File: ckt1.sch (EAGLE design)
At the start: 16 parts, among them J1 POWER_JACKSLT, M1 WIRELESS-NRF24L01-PA-EXT, U1 328P

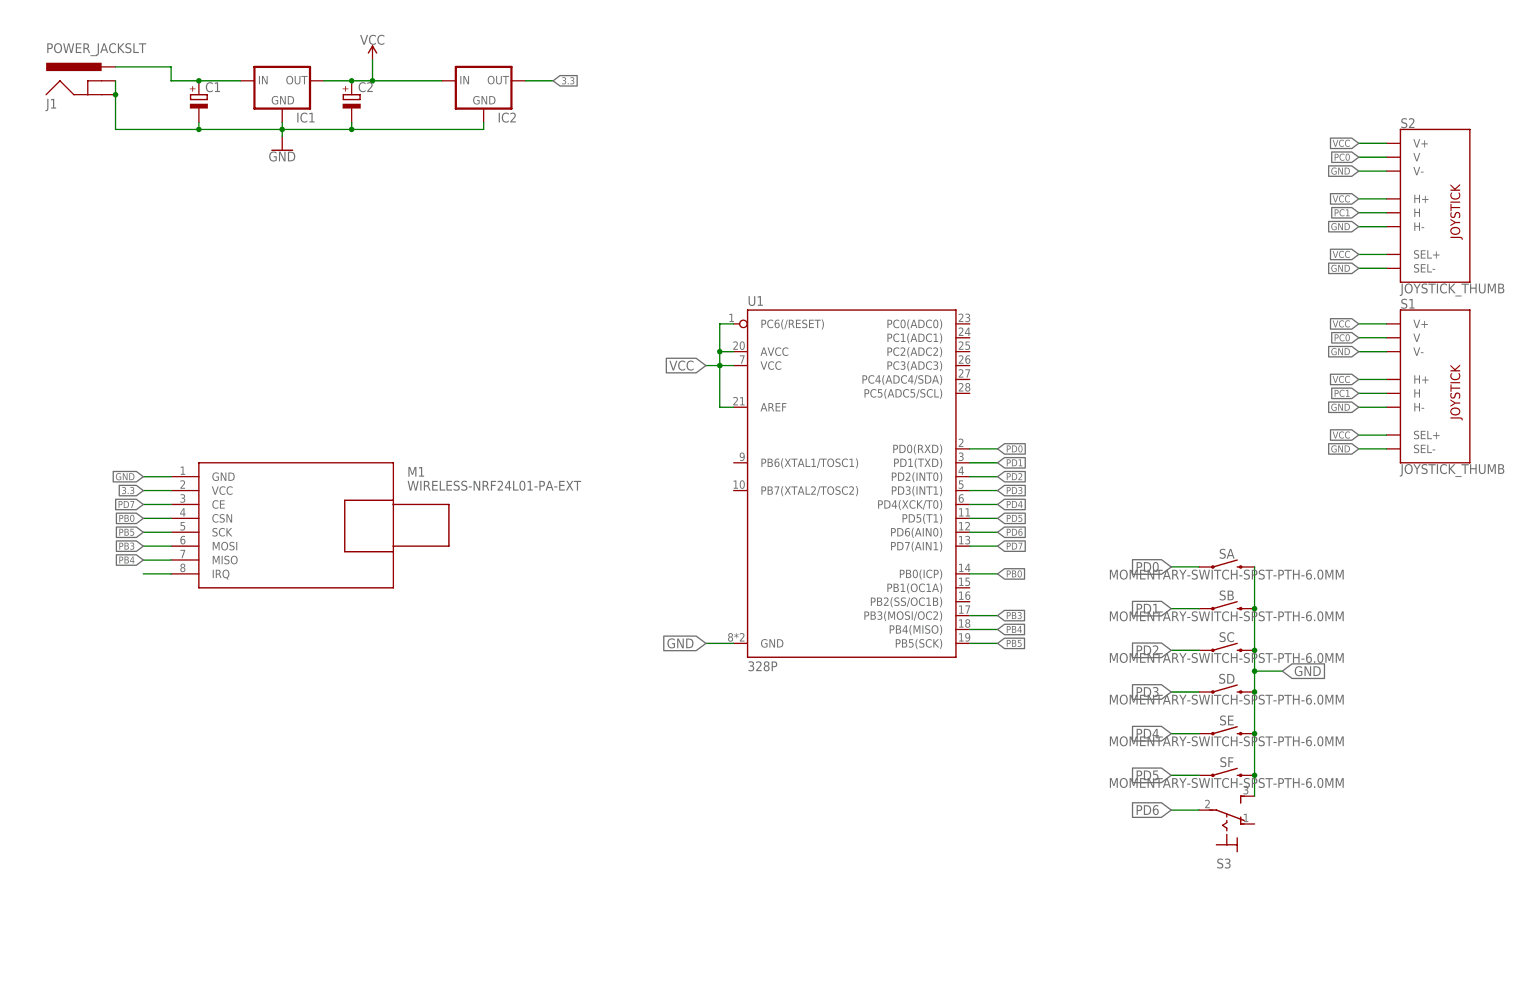
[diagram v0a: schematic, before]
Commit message: Formatting schematic and adding XTAL
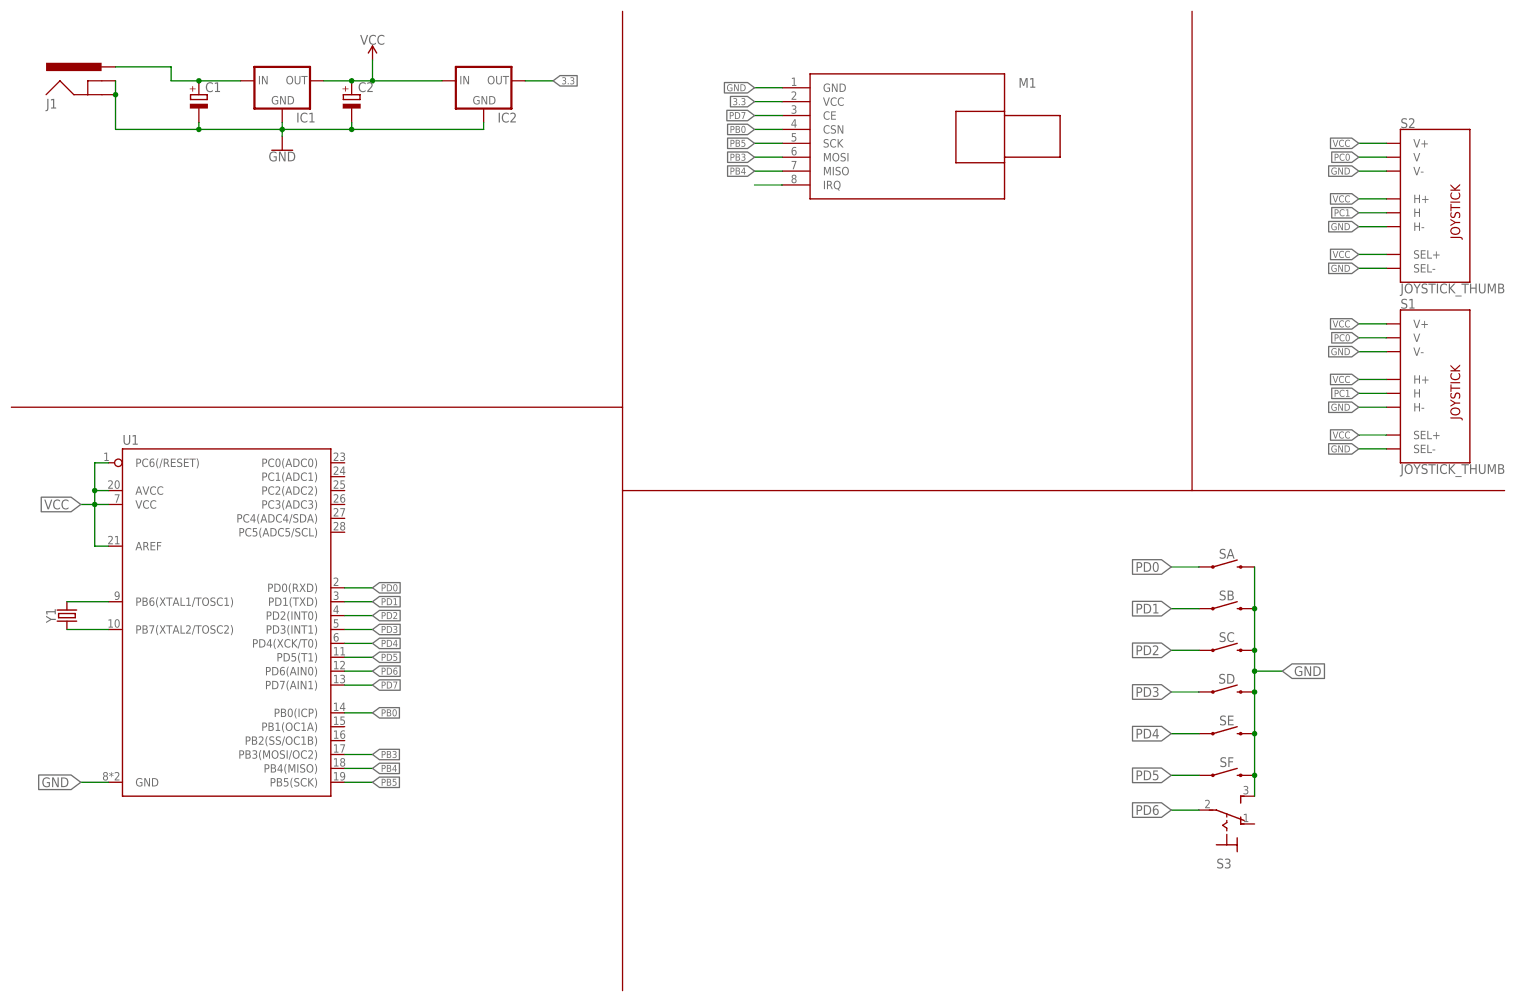
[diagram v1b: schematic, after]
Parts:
- added Y1: (no value), SparkFun-Clocks:CRYSTALPTH-HC49US
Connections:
- new net N$1: U1.PB6(XTAL1/TOSC1), Y1.2
- new net N$3: U1.PB7(XTAL2/TOSC2), Y1.1
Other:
- moved on the sheet: M1, U1

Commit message: Some changes to the board file
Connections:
- new net PC2: S1.V, U1.PC2(ADC2)
- new net PC3: S1.H, U1.PC3(ADC3)
- net GND: no longer S1.SEL-, S2.SEL-
- net PC0: now also U1.PC0(ADC0); no longer S1.V
- net PC1: now also U1.PC1(ADC1); no longer S1.H
- net VCC: no longer S1.SEL+, S2.SEL+
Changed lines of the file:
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@@
 <setting verticaltext="up"/>
 </settings>
-<grid distance="0.05" unitdist="inch" unit="inch" style="lines" multiple="1" display="yes" altdistance="0.005" altunitdist="inch" altunit="inch"/>
+<grid distance="0.1" unitdist="inch" unit="inch" style="lines" multiple="1" display="no" altdistance="0.01" altunitdist="inch" altunit="inch"/>
 <layers>
 <layer number="1" name="Top" color="4" fill="1" visible="no" active="no"/>
@@
 </segment>
 <segment>
-<pinref part="S2" gate="G$1" pin="SEL+"/>
-<wire x1="251.46" y1="134.62" x2="246.38" y2="134.62" width="0.1524" layer="91"/>
-<label x="246.38" y="134.62" size="1.27" layer="95" rot="R180" xref="yes"/>
-</segment>
-<segment>
 <pinref part="S1" gate="G$1" pin="V+"/>
 <wire x1="251.46" y1="121.92" x2="246.38" y2="121.92" width="0.1524" layer="91"/>
@@
 <wire x1="251.46" y1="111.76" x2="246.38" y2="111.76" width="0.1524" layer="91"/>
 <label x="246.38" y="111.76" size="1.27" layer="95" rot="R180" xref="yes"/>
-</segment>
-<segment>
-<pinref part="S1" gate="G$1" pin="SEL+"/>
-<wire x1="251.46" y1="101.6" x2="246.38" y2="101.6" width="0.1524" layer="91"/>
-<label x="246.38" y="101.6" size="1.27" layer="95" rot="R180" xref="yes"/>
 </segment>
 <segment>
@@
 </segment>
 <segment>
-<pinref part="S2" gate="G$1" pin="SEL-"/>
-<wire x1="251.46" y1="132.08" x2="246.38" y2="132.08" width="0.1524" layer="91"/>
-<label x="246.38" y="132.08" size="1.27" layer="95" rot="R180" xref="yes"/>
-</segment>
-<segment>
 <pinref part="S1" gate="G$1" pin="V-"/>
 <wire x1="251.46" y1="116.84" x2="246.38" y2="116.84" width="0.1524" layer="91"/>
@@
 <wire x1="251.46" y1="106.68" x2="246.38" y2="106.68" width="0.1524" layer="91"/>
 <label x="246.38" y="106.68" size="1.27" layer="95" rot="R180" xref="yes"/>
-</segment>
-<segment>
-<pinref part="S1" gate="G$1" pin="SEL-"/>
-<wire x1="251.46" y1="99.06" x2="246.38" y2="99.06" width="0.1524" layer="91"/>
-<label x="246.38" y="99.06" size="1.27" layer="95" rot="R180" xref="yes"/>
 </segment>
 <segment>
@@
 </segment>
 <segment>
-<pinref part="S1" gate="G$1" pin="V"/>
-<wire x1="251.46" y1="119.38" x2="246.38" y2="119.38" width="0.1524" layer="91"/>
-<label x="246.38" y="119.38" size="1.27" layer="95" rot="R180" xref="yes"/>
+<pinref part="U1" gate="U1" pin="PC0(ADC0)"/>
+<wire x1="60.96" y1="96.52" x2="66.04" y2="96.52" width="0.1524" layer="91"/>
+<label x="66.04" y="96.52" size="1.27" layer="95" xref="yes"/>
 </segment>
 </net>
@@
 </segment>
 <segment>
-<pinref part="S1" gate="G$1" pin="H"/>
-<wire x1="251.46" y1="109.22" x2="246.38" y2="109.22" width="0.1524" layer="91"/>
-<label x="246.38" y="109.22" size="1.27" layer="95" rot="R180" xref="yes"/>
+<pinref part="U1" gate="U1" pin="PC1(ADC1)"/>
+<wire x1="60.96" y1="93.98" x2="66.04" y2="93.98" width="0.1524" layer="91"/>
+<label x="66.04" y="93.98" size="1.27" layer="95" xref="yes"/>
 </segment>
 </net>
@@
 </segment>
 </net>
+<net name="PC2" class="0">
+<segment>
+<pinref part="U1" gate="U1" pin="PC2(ADC2)"/>
+<wire x1="60.96" y1="91.44" x2="66.04" y2="91.44" width="0.1524" layer="91"/>
+<label x="66.04" y="91.44" size="1.27" layer="95" xref="yes"/>
+</segment>
+<segment>
+<pinref part="S1" gate="G$1" pin="V"/>
+<wire x1="251.46" y1="119.38" x2="246.38" y2="119.38" width="0.1524" layer="91"/>
+<label x="246.38" y="119.38" size="1.27" layer="95" rot="R180" xref="yes"/>
+</segment>
+</net>
+<net name="PC3" class="0">
+<segment>
+<pinref part="U1" gate="U1" pin="PC3(ADC3)"/>
+<wire x1="60.96" y1="88.9" x2="66.04" y2="88.9" width="0.1524" layer="91"/>
+<label x="66.04" y="88.9" size="1.27" layer="95" xref="yes"/>
+</segment>
+<segment>
+<pinref part="S1" gate="G$1" pin="H"/>
+<wire x1="251.46" y1="109.22" x2="246.38" y2="109.22" width="0.1524" layer="91"/>
+<label x="246.38" y="109.22" size="1.27" layer="95" rot="R180" xref="yes"/>
+</segment>
+</net>
